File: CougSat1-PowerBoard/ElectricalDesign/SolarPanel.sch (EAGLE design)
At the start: 122 parts, among them J100 ADCS, J101 EPS, U1 INA199C2, U100 SPV1040, U101 SPV1040, U2 INA199C2, U3 INA199C2, U4 INA199C2, U5 AD7291, U6 AD7291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

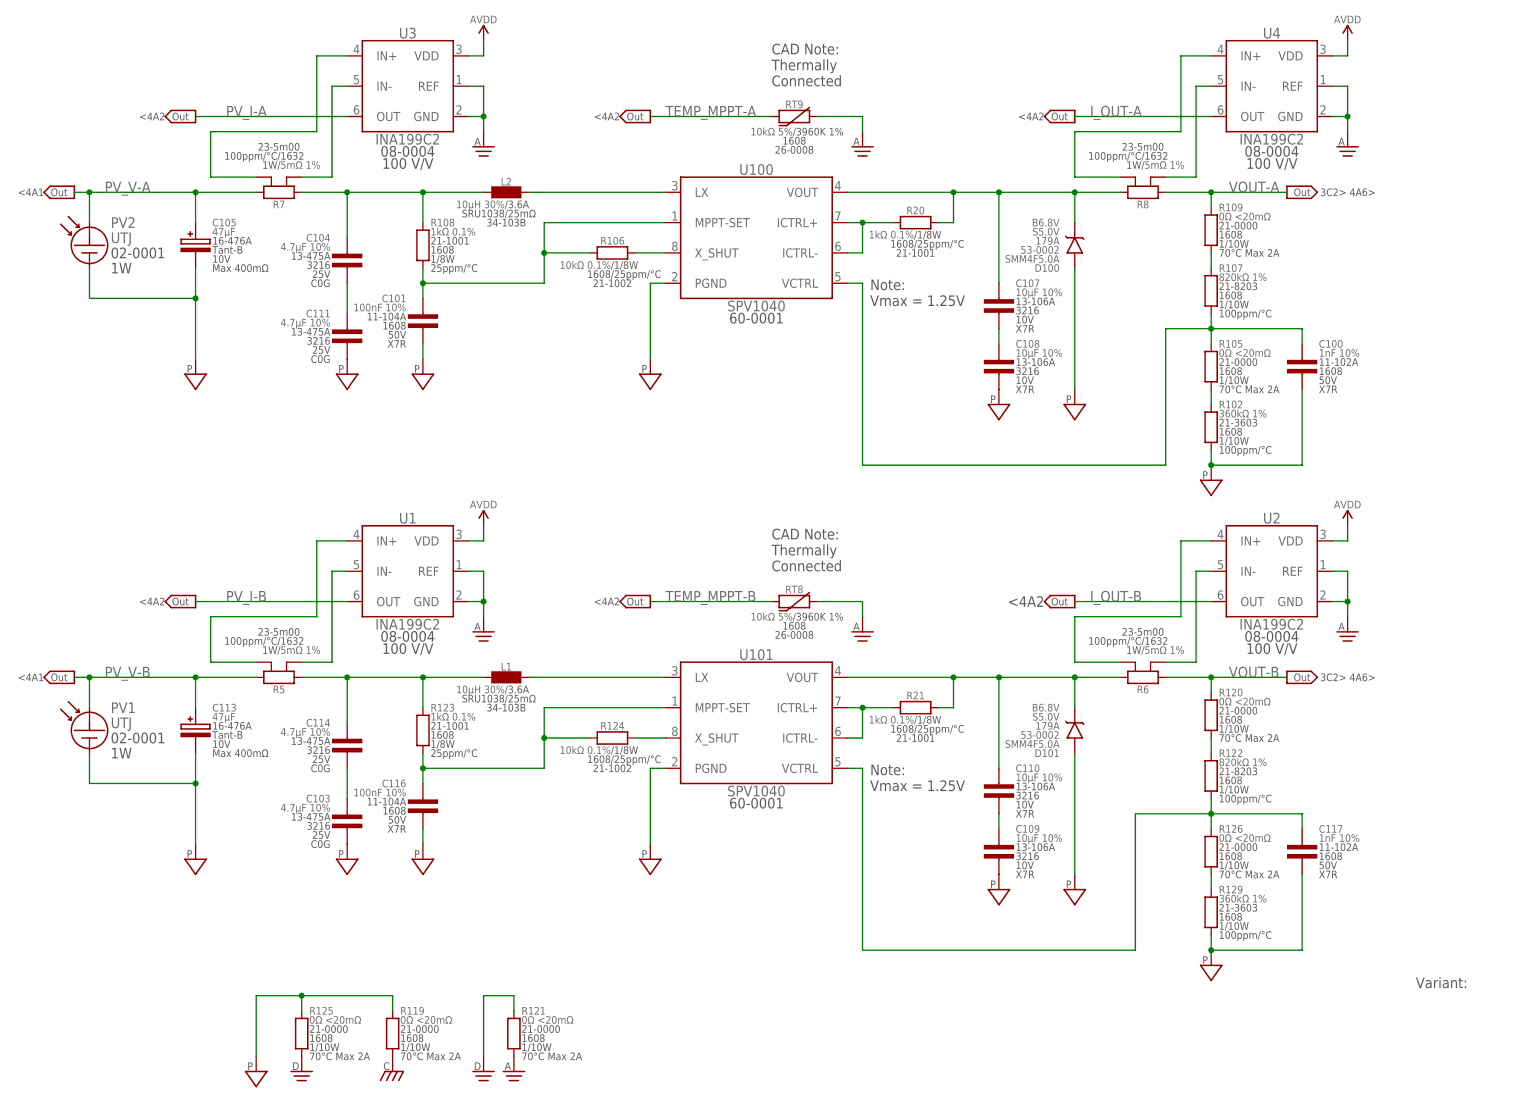
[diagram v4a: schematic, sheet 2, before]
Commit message: Addressed feedback, exported PDFs
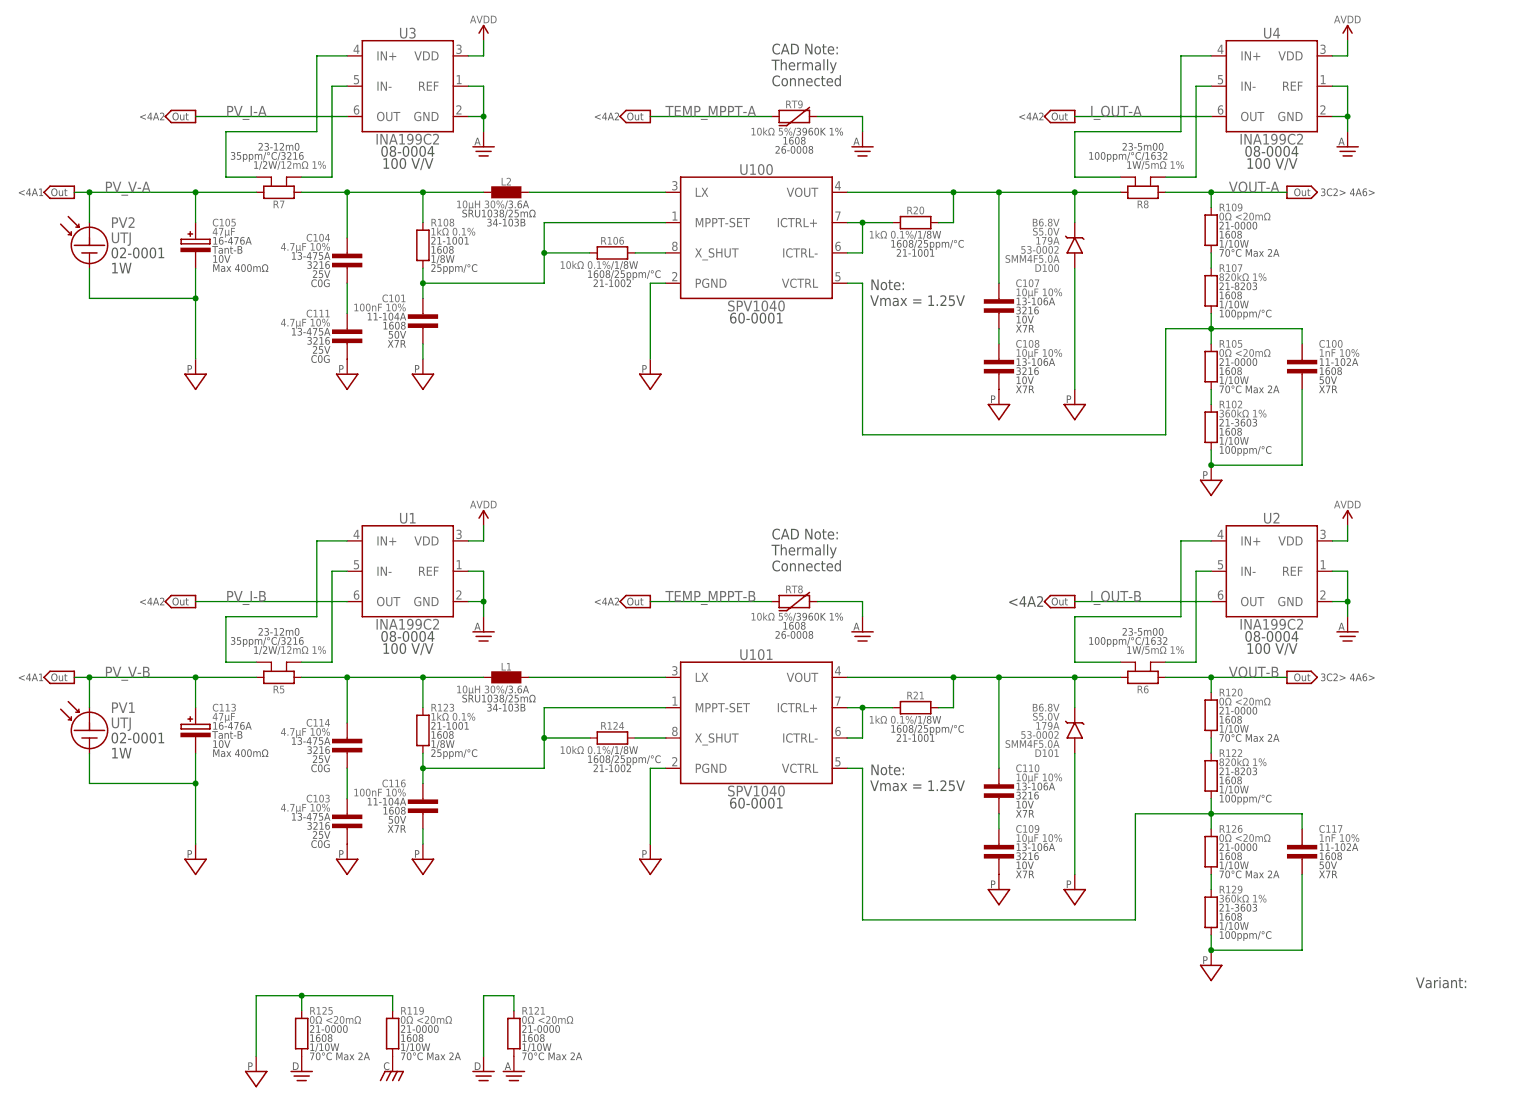
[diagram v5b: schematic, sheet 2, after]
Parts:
- R5, R7: value 5mΩ 1% -> 12mΩ 1%; device CougsInSpace-Resistors:RES-H-KELVIN-0.005R-1632 -> CougsInSpace-Resistors:RES-H-KELVIN-0.012R-3216

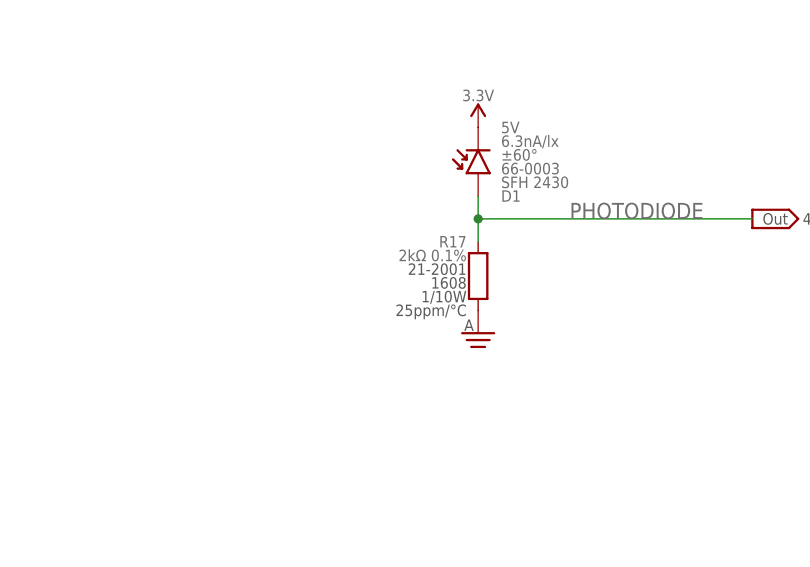
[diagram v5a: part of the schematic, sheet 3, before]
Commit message: Fixed photodiode circuit
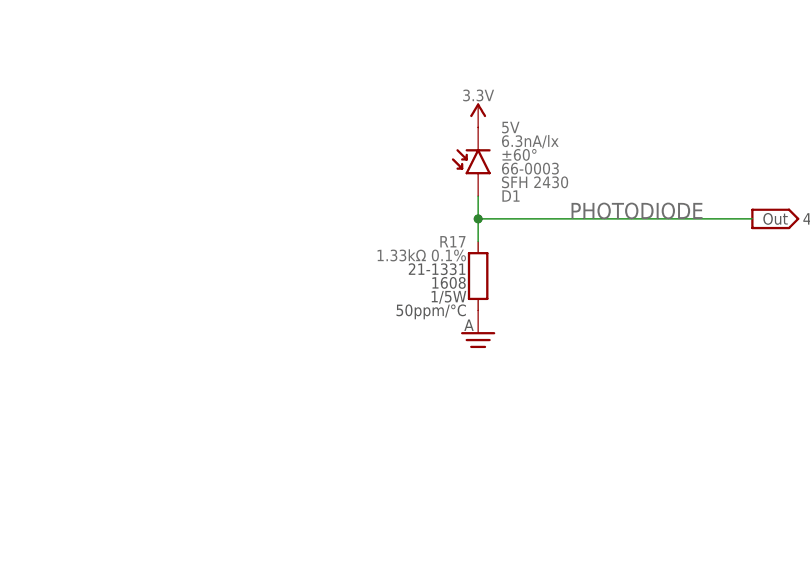
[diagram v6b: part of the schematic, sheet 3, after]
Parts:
- R17: value 2kΩ 0.1% -> 1.33kΩ 0.1%; device CougsInSpace-Resistors:RES-V-2K-1608 -> CougsInSpace-Resistors:RES-V-1.33K-1608
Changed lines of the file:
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@@
 <?xml version="1.0" encoding="utf-8"?>
 <!DOCTYPE eagle SYSTEM "eagle.dtd">
-<eagle version="9.5.1">
+<eagle version="9.5.2">
 <drawing>
 <settings>
@@
 <grid distance="0.1" unitdist="inch" unit="inch" style="lines" multiple="1" display="no" altdistance="0.01" altunitdist="inch" altunit="inch"/>
 <layers>
-<layer number="1" name="Top" color="4" fill="1" visible="no" active="no"/>
-<layer number="2" name="Route2" color="16" fill="1" visible="no" active="no"/>
-<layer number="3" name="Route3" color="17" fill="1" visible="no" active="no"/>
-<layer number="4" name="Route4" color="18" fill="1" visible="no" active="no"/>
-<layer number="5" name="Route5" color="19" fill="1" visible="no" active="no"/>
-<layer number="6" name="Route6" color="25" fill="1" visible="no" active="no"/>
-<layer number="7" name="Route7" color="26" fill="1" visible="no" active="no"/>
-<layer number="8" name="Route8" color="27" fill="1" visible="no" active="no"/>
-<layer number="9" name="Route9" color="28" fill="1" visible="no" active="no"/>
-<layer number="10" name="Route10" color="29" fill="1" visible="no" active="no"/>
-<layer number="11" name="Route11" color="30" fill="1" visible="no" active="no"/>
-<layer number="12" name="Route12" color="20" fill="1" visible="no" active="no"/>
-<layer number="13" name="Route13" color="21" fill="1" visible="no" active="no"/>
-<layer number="14" name="Route14" color="22" fill="1" visible="no" active="no"/>
-<layer number="15" name="Route15" color="23" fill="1" visible="no" active="no"/>
-<layer number="16" name="Bottom" color="1" fill="1" visible="no" active="no"/>
-<layer number="17" name="Pads" color="2" fill="1" visible="no" active="no"/>
-<layer number="18" name="Vias" color="2" fill="1" visible="no" active="no"/>
-<layer number="19" name="Unrouted" color="6" fill="1" visible="no" active="no"/>
-<layer number="20" name="Dimension" color="24" fill="1" visible="no" active="no"/>
-<layer number="21" name="tPlace" color="7" fill="1" visible="no" active="no"/>
-<layer number="22" name="bPlace" color="7" fill="1" visible="no" active="no"/>
-<layer number="23" name="tOrigins" color="15" fill="1" visible="no" active="no"/>
-<layer number="24" name="bOrigins" color="15" fill="1" visible="no" active="no"/>
-<layer number="25" name="tNames" color="7" fill="1" visible="no" active="no"/>
-<layer number="26" name="bNames" color="7" fill="1" visible="no" active="no"/>
-<layer number="27" name="tValues" color="7" fill="1" visible="no" active="no"/>
-<layer number="28" name="bValues" color="7" fill="1" visible="no" active="no"/>
+<layer number="1" name="Top" color="4" fill="1" visible="yes" active="no"/>
+<layer number="2" name="Route2" color="16" fill="1" visible="yes" active="no"/>
+<layer number="3" name="Route3" color="17" fill="1" visible="yes" active="no"/>
+<layer number="4" name="Route4" color="18" fill="1" visible="yes" active="no"/>
+<layer number="5" name="Route5" color="19" fill="1" visible="yes" active="no"/>
+<layer number="6" name="Route6" color="25" fill="1" visible="yes" active="no"/>
+<layer number="7" name="Route7" color="26" fill="1" visible="yes" active="no"/>
+<layer number="8" name="Route8" color="27" fill="1" visible="yes" active="no"/>
+<layer number="9" name="Route9" color="28" fill="1" visible="yes" active="no"/>
+<layer number="10" name="Route10" color="29" fill="1" visible="yes" active="no"/>
+<layer number="11" name="Route11" color="30" fill="1" visible="yes" active="no"/>
+<layer number="12" name="Route12" color="20" fill="1" visible="yes" active="no"/>
+<layer number="13" name="Route13" color="21" fill="1" visible="yes" active="no"/>
+<layer number="14" name="Route14" color="22" fill="1" visible="yes" active="no"/>
+<layer number="15" name="Route15" color="23" fill="1" visible="yes" active="no"/>
+<layer number="16" name="Bottom" color="1" fill="1" visible="yes" active="no"/>
+<layer number="17" name="Pads" color="2" fill="1" visible="yes" active="no"/>
+<layer number="18" name="Vias" color="2" fill="1" visible="yes" active="no"/>
+<layer number="19" name="Unrouted" color="6" fill="1" visible="yes" active="no"/>
+<layer number="20" name="Dimension" color="24" fill="1" visible="yes" active="no"/>
+<layer number="21" name="tPlace" color="7" fill="1" visible="yes" active="no"/>
+<layer number="22" name="bPlace" color="7" fill="1" visible="yes" active="no"/>
+<layer number="23" name="tOrigins" color="15" fill="1" visible="yes" active="no"/>
+<layer number="24" name="bOrigins" color="15" fill="1" visible="yes" active="no"/>
+<layer number="25" name="tNames" color="7" fill="1" visible="yes" active="no"/>
+<layer number="26" name="bNames" color="7" fill="1" visible="yes" active="no"/>
+<layer number="27" name="tValues" color="7" fill="1" visible="yes" active="no"/>
+<layer number="28" name="bValues" color="7" fill="1" visible="yes" active="no"/>
 <layer number="29" name="tStop" color="7" fill="3" visible="no" active="no"/>
 <layer number="30" name="bStop" color="7" fill="6" visible="no" active="no"/>
@@
 <layer number="35" name="tGlue" color="7" fill="4" visible="no" active="no"/>
 <layer number="36" name="bGlue" color="7" fill="5" visible="no" active="no"/>
-<layer number="37" name="tTest" color="7" fill="1" visible="no" active="no"/>
-<layer number="38" name="bTest" color="7" fill="1" visible="no" active="no"/>
+<layer number="37" name="tTest" color="7" fill="1" visible="yes" active="no"/>
+<layer number="38" name="bTest" color="7" fill="1" visible="yes" active="no"/>
 <layer number="39" name="tKeepout" color="4" fill="11" visible="no" active="no"/>
 <layer number="40" name="bKeepout" color="1" fill="11" visible="no" active="no"/>
@@
 <layer number="44" name="Drills" color="7" fill="1" visible="no" active="no"/>
 <layer number="45" name="Holes" color="7" fill="1" visible="no" active="no"/>
-<layer number="46" name="Milling" color="3" fill="1" visible="no" active="no"/>
-<layer number="47" name="Measures" color="7" fill="1" visible="no" active="no"/>
-<layer number="48" name="Document" color="7" fill="1" visible="no" active="no"/>
-<layer number="49" name="Reference" color="7" fill="1" visible="no" active="no"/>
-<layer number="50" name="dxf" color="7" fill="1" visible="no" active="no"/>
-<layer number="51" name="tDocu" color="7" fill="1" visible="no" active="no"/>
-<layer number="52" name="bDocu" color="7" fill="1" visible="no" active="no"/>
-<layer number="53" name="tGND_GNDA" color="7" fill="9" visible="no" active="no"/>
-<layer number="54" name="bGND_GNDA" color="1" fill="9" visible="no" active="no"/>
-<layer number="56" name="wert" color="7" fill="1" visible="no" active="no"/>
-<layer number="57" name="tCAD" color="7" fill="1" visible="no" active="no"/>
-<layer number="58" name="bCAD" color="9" fill="1" visible="no" active="no"/>
-<layer number="59" name="tCarbon" color="7" fill="1" visible="no" active="no"/>
-<layer number="60" name="bCarbon" color="7" fill="1" visible="no" active="no"/>
+<layer number="46" name="Milling" color="3" fill="1" visible="yes" active="no"/>
+<layer number="47" name="Measures" color="7" fill="1" visible="yes" active="no"/>
+<layer number="48" name="Document" color="7" fill="1" visible="yes" active="no"/>
+<layer number="49" name="Reference" color="7" fill="1" visible="yes" active="no"/>
+<layer number="50" name="dxf" color="7" fill="1" visible="yes" active="no"/>
+<layer number="51" name="tDocu" color="7" fill="1" visible="yes" active="no"/>
+<layer number="52" name="bDocu" color="7" fill="1" visible="yes" active="no"/>
+<layer number="53" name="tGND_GNDA" color="7" fill="9" visible="yes" active="no"/>
+<layer number="54" name="bGND_GNDA" color="1" fill="9" visible="yes" active="no"/>
+<layer number="56" name="wert" color="7" fill="1" visible="yes" active="no"/>
+<layer number="57" name="tCAD" color="7" fill="1" visible="yes" active="no"/>
+<layer number="58" name="bCAD" color="9" fill="1" visible="yes" active="no"/>
+<layer number="59" name="tCarbon" color="7" fill="1" visible="yes" active="no"/>
+<layer number="60" name="bCarbon" color="7" fill="1" visible="yes" active="no"/>
 <layer number="88" name="SimResults" color="9" fill="1" visible="yes" active="yes"/>
 <layer number="89" name="SimProbes" color="9" fill="1" visible="yes" active="yes"/>
@@
 <part name="TP3" library="CougsInSpace-Connectors" deviceset="TEST_POINT" device="-THT-1.0"/>
 <part name="TP4" library="CougsInSpace-Connectors" deviceset="TEST_POINT" device="-THT-1.0"/>
-<part name="R17" library="CougsInSpace-Resistors" deviceset="RES-V" device="-1608" technology="-2K" value="2kΩ 0.1%"/>
+<part name="R17" library="CougsInSpace-Resistors" deviceset="RES-V" device="-1608" technology="-1.33K" value="1.33kΩ 0.1%"/>
 <part name="SUPPLY24" library="CougsInSpace-PowerSymbols" deviceset="3.3V" device=""/>
 <part name="OFFSHEET31" library="CougsInSpace-Aesthetics" deviceset="OFF_SHEET-OUT" device=""/>

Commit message: Addressed all feedback
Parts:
- removed C12, C14: 1µF 10%, CougsInSpace-Capacitors:CAP-V-1UF-1608
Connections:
- net AGND: no longer C12.2, C14.2
- net AVREF-0: no longer C12.1
- net AVREF-1: no longer C14.1
